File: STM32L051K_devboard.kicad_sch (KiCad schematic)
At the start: 11 parts, among them J1 Conn_01x16_Pin, J2 Conn_01x16_Pin, J3 Conn_01x05_Pin, U1 STM32L051K8Ux

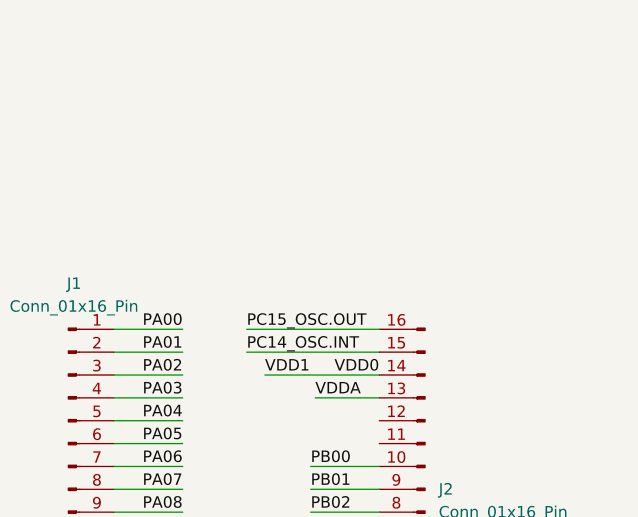
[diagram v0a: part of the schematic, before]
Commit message: Agregado XTAL low power y pines clock removidos
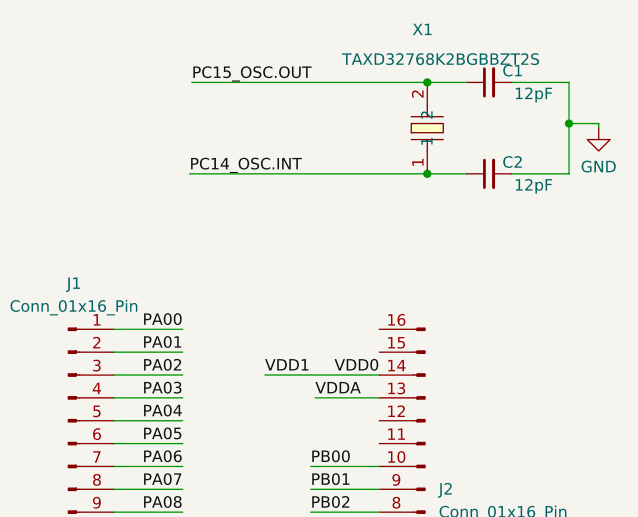
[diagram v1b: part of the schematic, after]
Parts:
- added C1, C2: 12pF, Capacitor_SMD:C_0603_1608Metric, symbol Device:C_Small
- added X1: TAXD32768K2BGBBZT2S, EasyEDA:OSC-TH_BD2.0-P0.70-D0.3, symbol EasyEDA:TAXD32768K2BGBBZT2S
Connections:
- net GND: now also C1.2, C2.2
- net PC14_OSC.INT: now also C2.1, X1.1; no longer J2.15 (Pin_15)
- net PC15_OSC.OUT: now also C1.1, X1.2; no longer J2.16 (Pin_16)

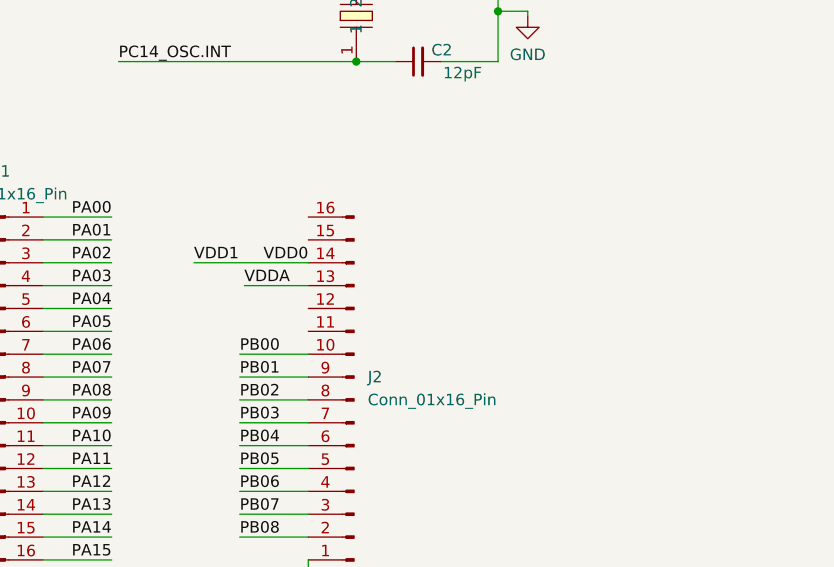
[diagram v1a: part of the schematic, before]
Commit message: agregado LDO y VDDA puenteado a 3.3
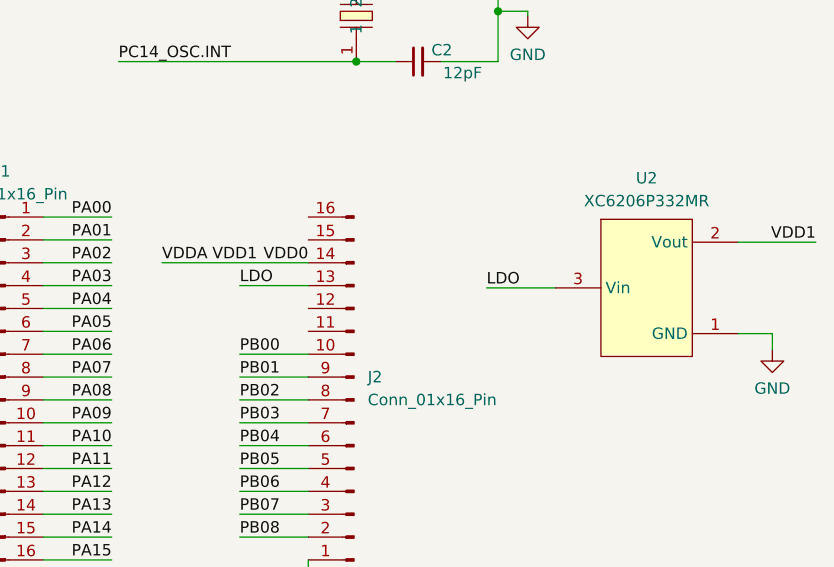
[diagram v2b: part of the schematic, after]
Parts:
- added U2: XC6206P332MR, EasyEDA:SOT-23-3_L2.9-W1.6-P1.90-LS2.8-BR, symbol EasyEDA:XC6206P332MR
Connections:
- net GND: now also U2.1 (GND)
- net VDD0: now also C4.1, U1.5 (VDDA), U2.2 (Vout)
- removed net VDDA: C4.1, J2.13 (Pin_13), U1.5 (VDDA)
- new net LDO: J2.13 (Pin_13), U2.3 (Vin)
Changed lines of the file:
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@@
+	(wire
+		(pts
+			(xy 198.12 74.93) (xy 214.376 74.93)
+		)
+		(stroke
+			(width 0)
+			(type default)
+		)
+	)
 	(wire
 		(pts
@@
 	(wire
 		(pts
+			(xy 265.938 84.582) (xy 265.938 82.804)
+		)
+		(stroke
+			(width 0)
+			(type default)
+		)
+	)
+	(wire
+		(pts
 			(xy 109.982 67.818) (xy 117.602 67.818)
 		)
@@
 	(wire
 		(pts
-			(xy 201.676 74.93) (xy 214.376 74.93)
-		)
-		(stroke
-			(width 0)
-			(type default)
-		)
-	)
-	(wire
-		(pts
 			(xy 155.702 72.898) (xy 148.082 72.898)
 		)
@@
 	(wire
 		(pts
+			(xy 206.756 77.47) (xy 214.376 77.47)
+		)
+		(stroke
+			(width 0)
+			(type default)
+		)
+	)
+	(wire
+		(pts
 			(xy 155.702 77.978) (xy 148.082 77.978)
 		)
@@
 	(wire
 		(pts
-			(xy 207.264 77.47) (xy 214.376 77.47)
-		)
-		(stroke
-			(width 0)
-			(type default)
-		)
-	)
-	(wire
-		(pts
 			(xy 109.982 90.678) (xy 117.602 90.678)
 		)
@@
 	(wire
 		(pts
+			(xy 265.938 82.804) (xy 262.128 82.804)
+		)
+		(stroke
+			(width 0)
+			(type default)
+		)
+	)
+	(wire
+		(pts
 			(xy 193.294 52.578) (xy 219.71 52.578)
 		)
@@
 	(wire
 		(pts
+			(xy 234.188 77.724) (xy 241.808 77.724)
+		)
+		(stroke
+			(width 0)
+			(type default)
+		)
+	)
+	(wire
+		(pts
 			(xy 109.982 95.758) (xy 117.602 95.758)
 		)
@@
 		(pts
 			(xy 164.084 98.298) (xy 162.306 98.298)
+		)
+		(stroke
+			(width 0)
+			(type default)
+		)
+	)
+	(wire
+		(pts
+			(xy 270.764 72.644) (xy 262.128 72.644)
 		)
 		(stroke
@@
 		)
 	)
+	(label "VDDA"
+		(at 198.12 74.93 0)
+		(effects
+			(font
+				(size 1.27 1.27)
+			)
+			(justify left bottom)
+		)
+	)
 	(label "PA05"
 		(at 109.982 90.678 0)
@@
 		)
 	)
+	(label "LDO"
+		(at 234.188 77.724 0)
+		(effects
+			(font
+				(size 1.27 1.27)
+			)
+			(justify left bottom)
+		)
+	)
 	(label "PA13"
 		(at 109.982 70.358 0)
@@
 		)
 	)
+	(label "LDO"
+		(at 206.756 77.47 0)
+		(effects
+			(font
+				(size 1.27 1.27)
+			)
+			(justify left bottom)
+		)
+	)
 	(label "PB01"
 		(at 155.702 83.058 180)
@@
 	)
 	(label "VDD1"
-		(at 201.676 74.93 0)
+		(at 203.708 74.93 0)
 		(effects
 			(font
@@
 		)
 	)
-	(label "VDDA"
-		(at 207.264 77.47 0)
-		(effects
-			(font
-				(size 1.27 1.27)
-			)
-			(justify left bottom)
-		)
-	)
 	(label "PB02"
 		(at 155.702 80.518 180)
@@
 	(label "PA13"
 		(at 199.39 113.792 270)
+		(effects
+			(font
+				(size 1.27 1.27)
+			)
+			(justify right bottom)
+		)
+	)
+	(label "VDD1"
+		(at 270.764 72.644 180)
 		(effects
 			(font
@@
 	(symbol
 		(lib_id "power:GND")
+		(at 265.938 84.582 0)
+		(unit 1)
+		(exclude_from_sim no)
+		(in_bom yes)
+		(on_board yes)
+		(dnp no)
+		(fields_autoplaced yes)
+		(property "Reference" "#PWR09"
+			(at 265.938 90.932 0)
+			(effects
+				(font
+					(size 1.27 1.27)
+				)
+				(hide yes)
+			)
+		)
+		(property "Value" "GND"
+			(at 265.938 88.9 0)
+			(effects
+				(font
+					(size 1.27 1.27)
+				)
+			)
+		)
+		(property "Footprint" ""
+			(at 265.938 84.582 0)
+			(effects
+				(font
+					(size 1.27 1.27)
+				)
+				(hide yes)
+			)
+		)
+		(property "Datasheet" ""
+			(at 265.938 84.582 0)
+			(effects
+				(font
+					(size 1.27 1.27)
+				)
+				(hide yes)
+			)
+		)
+		(property "Description" "Power symbol creates a global label with name \"GND\" , ground"
+			(at 265.938 84.582 0)
+			(effects
+				(font
+					(size 1.27 1.27)
+				)
+				(hide yes)
+			)
+		)
+		(pin "1"
+		)
+		(instances
+			(project "STM32L051K_devboard"
+				(path "/dd525c43-ed51-4d3d-a54d-1a171726872e"
+					(reference "#PWR09")
+					(unit 1)
+				)
+			)
+		)
+	)
+	(symbol
+		(lib_id "power:GND")
 		(at 214.376 110.236 0)
 		(unit 1)
@@
 					(unit 1)
 				)
+			)
+		)
+	)
+	(symbol
+		(lib_id "EasyEDA:XC6206P332MR")
+		(at 251.968 77.724 0)
+		(unit 1)
+		(exclude_from_sim no)
+		(in_bom yes)
+		(on_board yes)
+		(dnp no)
+		(fields_autoplaced yes)
+		(property "Reference" "U2"
+			(at 251.968 65.532 0)
+			(effects
+				(font
+					(size 1.27 1.27)
+				)
+			)
+		)
+		(property "Value" "XC6206P332MR"
+			(at 251.968 68.072 0)
+			(effects
+				(font
+					(size 1.27 1.27)
+				)
+			)
+		)
+		(property "Footprint" "EasyEDA:SOT-23-3_L2.9-W1.6-P1.90-LS2.8-BR"
+			(at 251.968 90.424 0)
+			(effects
+				(font
+					(size 1.27 1.27)
+				)
+				(hide yes)
+			)
+		)
+		(property "Datasheet" "https://lcsc.com/product-detail/Low-Dropout-Regulators-LDO_XC6206P332MR_C5446.html"
+			(at 251.968 92.964 0)
+			(effects
+				(font
+					(size 1.27 1.27)
+				)
+				(hide yes)
+			)
+		)
+		(property "Description" ""
+			(at 251.968 77.724 0)
+			(effects
+				(font
+					(size 1.27 1.27)
+				)
+				(hide yes)
+			)
+		)
+		(property "Manufacturer" "TOREX(特瑞仕)"
+			(at 251.968 95.504 0)
+			(effects
+				(font
+					(size 1.27 1.27)
+				)
+				(hide yes)
+			)
+		)
+		(property "MPN" "XC6206P332MR-G"
+			(at 251.968 98.044 0)
+			(effects
+				(font
+					(size 1.27 1.27)
+				)
+				(hide yes)
+			)
+		)
+		(property "LCSC Part" "C5446"
+			(at 251.968 100.584 0)
+			(effects
+				(font
+					(size 1.27 1.27)
+				)
+				(hide yes)
+			)
+		)
+		(pin "1"
+		)
+		(pin "3"
+		)
+		(pin "2"
+		)
+		(instances
+			(project ""
+				(path "/dd525c43-ed51-4d3d-a54d-1a171726872e"
+					(reference "U2")
+					(unit 1)
+				)

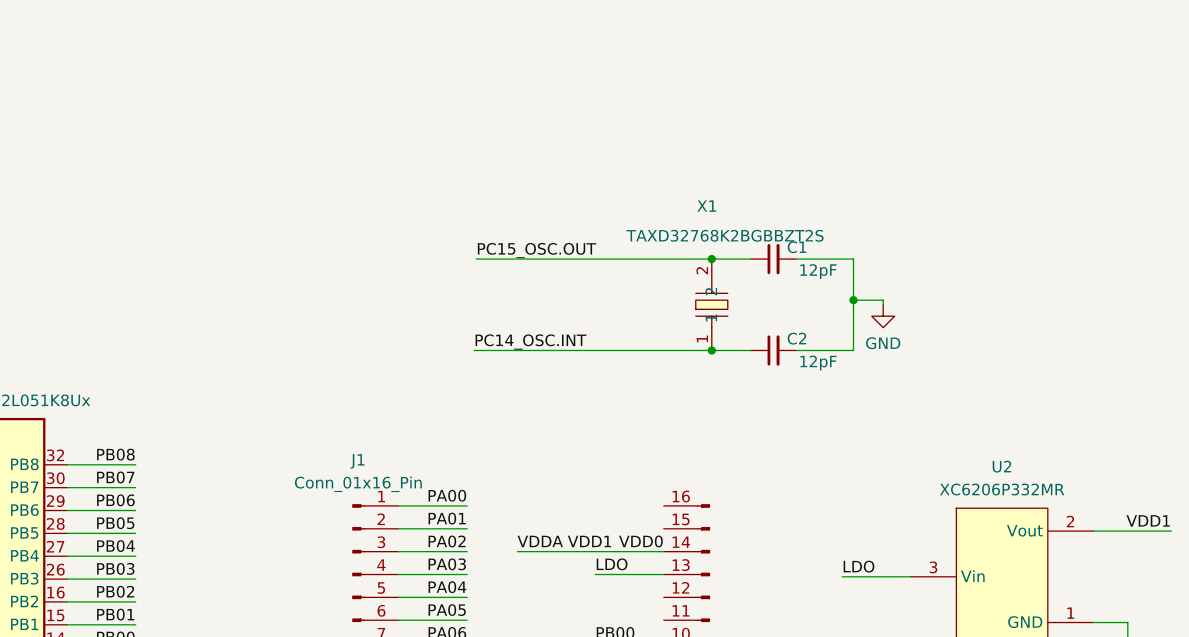
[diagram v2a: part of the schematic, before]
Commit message: cambio de crital a SMD 8 MHz
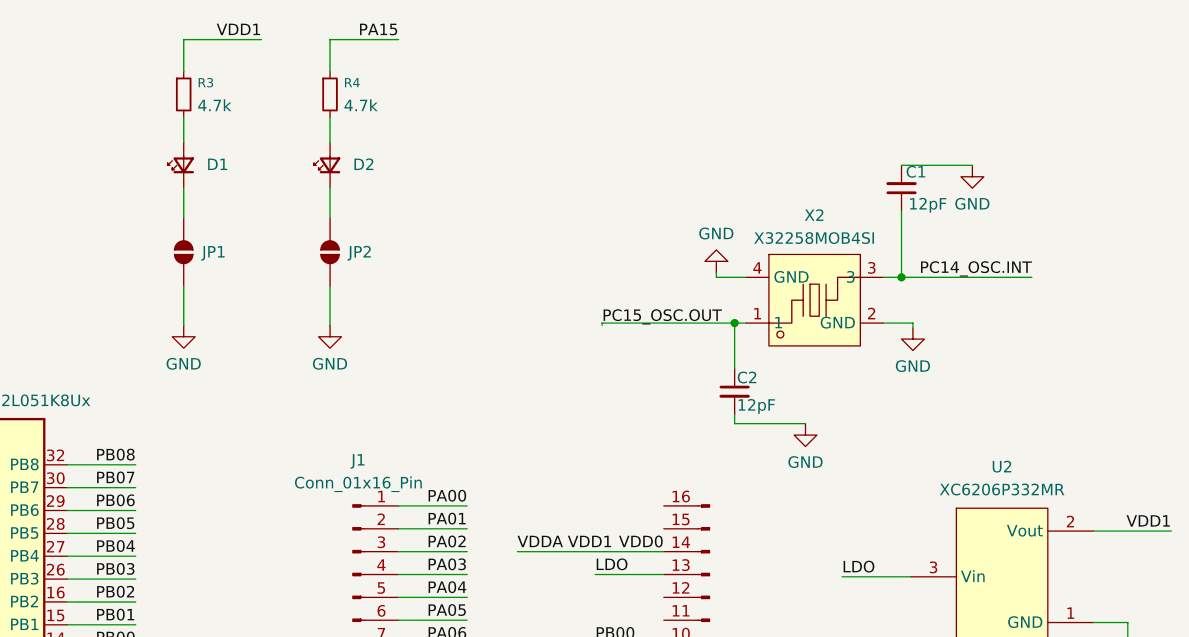
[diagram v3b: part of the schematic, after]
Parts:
- removed X1: TAXD32768K2BGBBZT2S, EasyEDA:OSC-TH_BD2.0-P0.70-D0.3, symbol EasyEDA:TAXD32768K2BGBBZT2S
- added D1, D2: LED_Small, LED_SMD:LED_0603_1608Metric, symbol Device:LED_Small
- added JP1, JP2: SolderJumper_2_Open, Jumper:SolderJumper-2_P1.3mm_Open_TrianglePad1.0x1.5mm, symbol Jumper:SolderJumper_2_Open
- added R3, R4: 4.7k, Resistor_SMD:R_0603_1608Metric, symbol Device:R_Small
- added X2: X32258MOB4SI, EasyEDA:CRYSTAL-SMD_4P-L3.2-W2.5-BL, symbol EasyEDA:X32258MOB4SI
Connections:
- net GND: now also JP1.1 (A), JP2.1 (A), X2.2 (GND), X2.4 (GND)
- net PA15: now also R4.1
- net PC14_OSC.INT: now also C1.1, X2.3; no longer C2.1
- net PC15_OSC.OUT: now also C2.1, X2.1; no longer C1.1
- net VDD0: now also R3.1
- new net: D2.2 (A), R4.2
- new net: D1.2 (A), R3.2
- new net: D2.1 (K), JP2.2 (B)
- new net: D1.1 (K), JP1.2 (B)
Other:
- moved on the sheet: C1, C2
